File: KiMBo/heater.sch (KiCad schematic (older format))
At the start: 61 parts, among them Q10 DMP3098L-7, Q11 2N7002, Q12 2N7002, Q13 DMP3098L-7, Q14 DMP3098L-7, Q5 2N7002, Q6 IPD90P03P4-04, Q7 2N7002, Q8 2N7002, Q9 DMP3098L-7

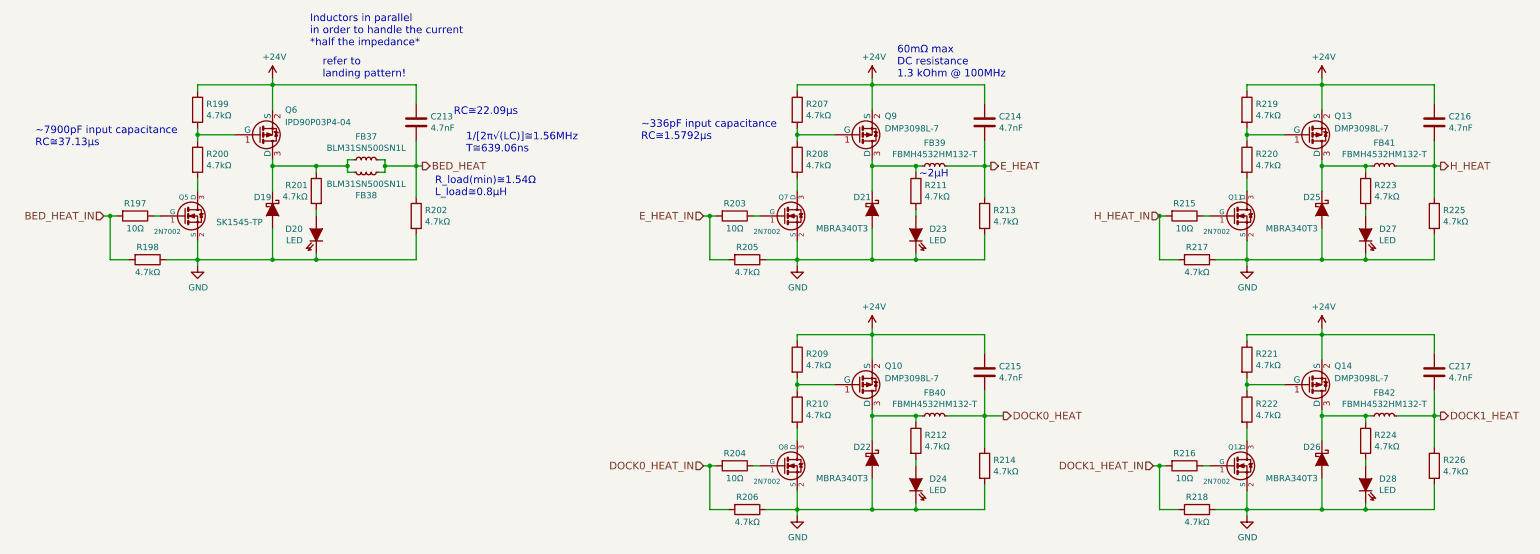
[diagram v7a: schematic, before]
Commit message: Remove HDMI from the schematic
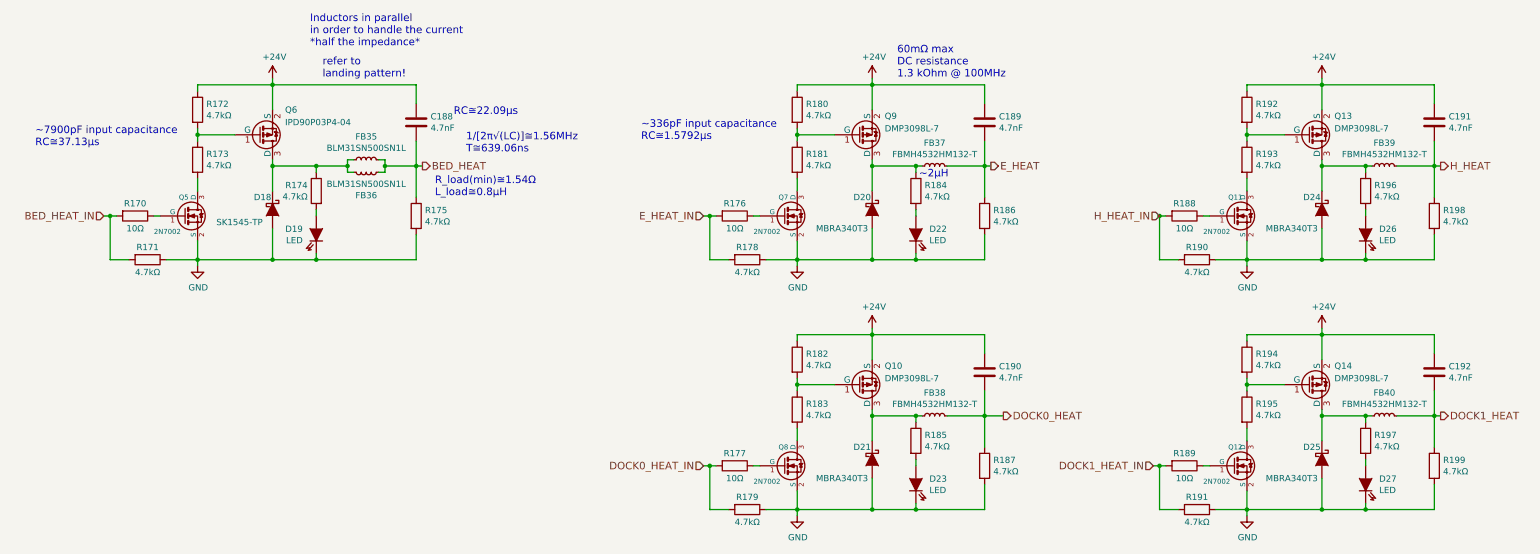
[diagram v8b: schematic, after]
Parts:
- renumbered C213 to C188, C214 to C189, C215 to C190, C216 to C191, C217 to C192, D19 to D18, D20 to D19, D21 to D20, D22 to D21, D23 to D22, D24 to D23, D25 to D24, D26 to D25, D27 to D26, D28 to D27, FB37 to FB35, FB38 to FB36, FB39 to FB37, FB40 to FB38, FB41 to FB39, FB42 to FB40, R197 to R170, R198 to R171, R199 to R172, R200 to R173, R201 to R174, R202 to R175, R203 to R176, R204 to R177, R205 to R178, R206 to R179, R207 to R180, R208 to R181, R209 to R182, R210 to R183, R211 to R184, R212 to R185, R213 to R186, R214 to R187, R215 to R188, R216 to R189, R217 to R190, R218 to R191, R219 to R192, R220 to R193, R221 to R194, R222 to R195, R223 to R196, R224 to R197, R225 to R198, R226 to R199
